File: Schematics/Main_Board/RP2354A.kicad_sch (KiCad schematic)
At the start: 39 parts, among them J1 USB4105-GF-A, J4 DEBUG, U1 RP2354A, U2 MCP1702T-3302E_CB, X1 IQXO-791_12MHz

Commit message: organizational changes to schematic
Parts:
- removed J1: USB4105-GF-A, Eclectronics:USB4105-GF-A, symbol Eclectronics:USB4105-GF-A
- removed R3, R4: 5.1K, Resistor_SMD:R_0402_1005Metric, symbol Device:R
- removed R5, R6: 27Ω, Resistor_SMD:R_0402_1005Metric, symbol Device:R
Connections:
- no-connect marks 9 -> 7
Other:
- note removed: "USB-C Connector"
- moved on the sheet: C5, J4, R1, R2, S1, S2, X1

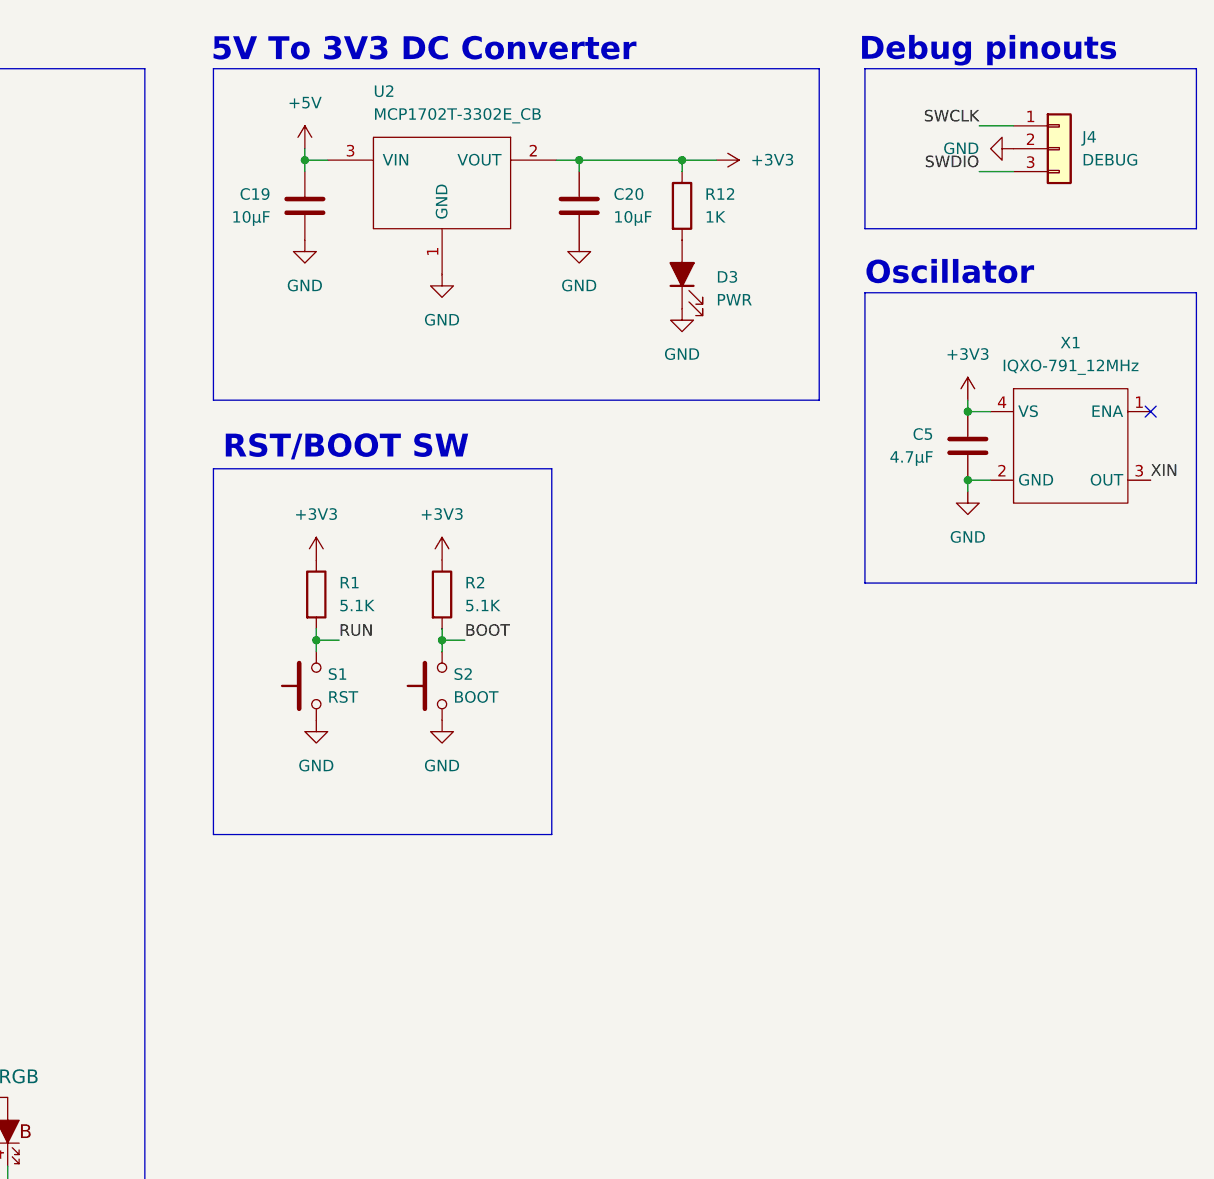
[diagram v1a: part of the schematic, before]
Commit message: Added initial Lipo Charger and BMS, reorganized footprint library and merged symbol libraries
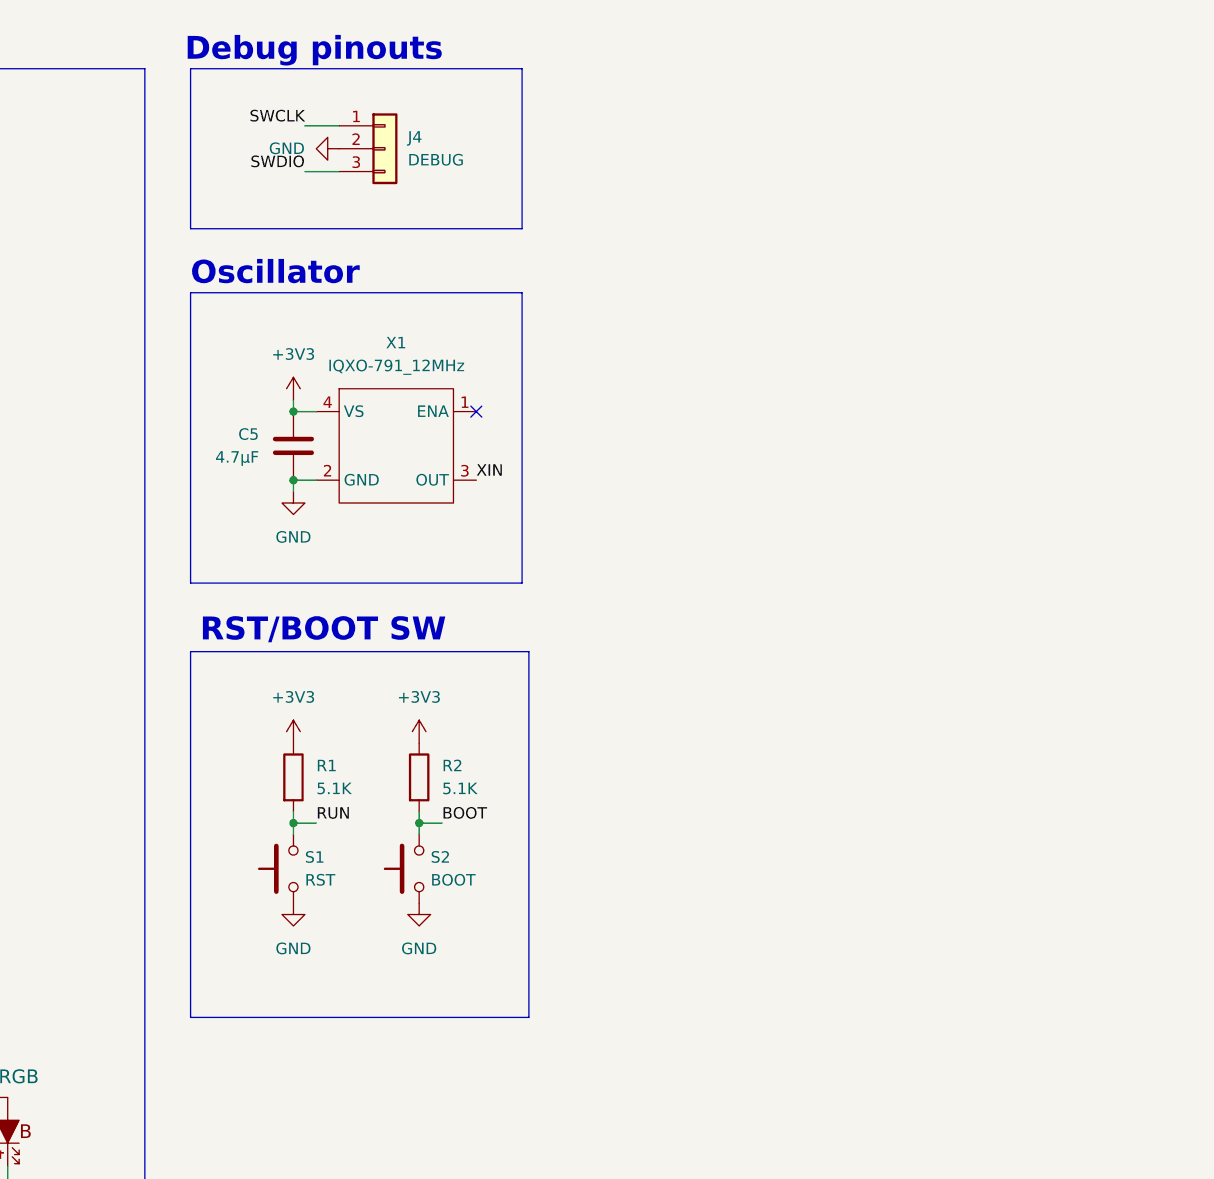
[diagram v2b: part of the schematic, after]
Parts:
- removed C19, C20: 10µF, Capacitor_SMD:C_0603_1608Metric, symbol Device:C
- removed D3: PWR, LED_SMD:LED_0805_2012Metric, symbol Device:LED_Filled
- removed R12: 1K, Resistor_SMD:R_0402_1005Metric, symbol Device:R
- removed U2: MCP1702T-3302E_CB, Eclectronics:SOT-23A_MC_MCH, symbol Eclectronics:MCP1702T-3302E_CB
- D2: footprint Eclectronics:IN-S85TATRGB -> PU_Lib:IN-S85TATRGB; symbol Eclectronics:IN-S85TATRGB -> PU_Lib:IN-S85TATRGB
- L2: footprint Eclectronics:AOTA-B201610S3R3-101-T -> PU_Lib:AOTA-B201610S3R3-101-T; symbol Eclectronics:AOTA-B201610S3R3-101-T -> PU_Lib:AOTA-B201610S3R3-101-T
- S1, S2: symbol Eclectronics:SW -> PU_Lib:SW
- U1: footprint Eclectronics:RP2350A_QFN-60_EP_7.75x7.75_Pitch0.4mm -> PU_Lib:RP2350A_QFN-60_EP_7.75x7.75_Pitch0.4mm; symbol Eclectronics:RP2350A -> PU_Lib:RP2350A
- X1: footprint Eclectronics:IQXO-791 -> PU_Lib:IQXO-791; symbol Eclectronics:IQXO-791 -> PU_Lib:IQXO-791
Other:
- note removed: "5V To 3V3 DC Converter"
- moved on the sheet: C5, J4, R1, R2, S1, S2, X1
